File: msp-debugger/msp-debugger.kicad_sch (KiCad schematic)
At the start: 12 parts, among them J1 USB_B_Mini, J2 Conn_02x10, SW1 SW_MEC_5E, SW2 SW_MEC_5E, SW3 SW_MEC_5E, SW4 SW_MEC_5E, U1 ESP32-WROOM-32, U2 NHD-0420H1Z

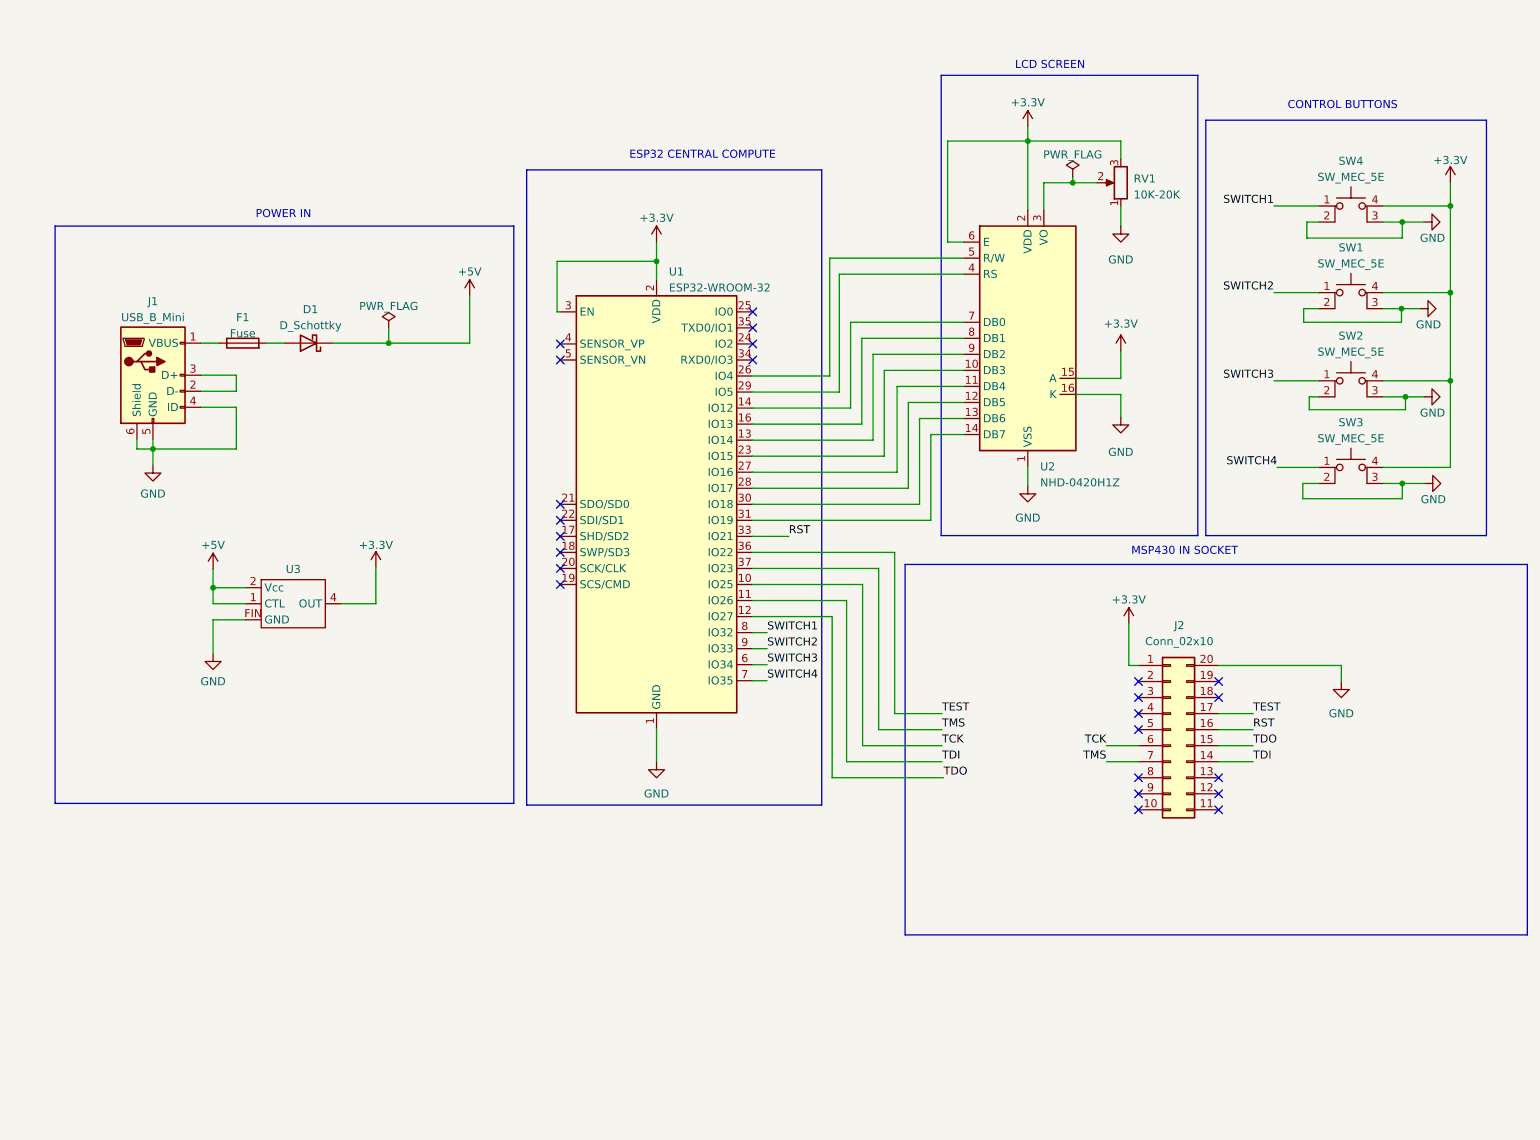
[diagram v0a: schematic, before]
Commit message: use digikey/espressif libraries
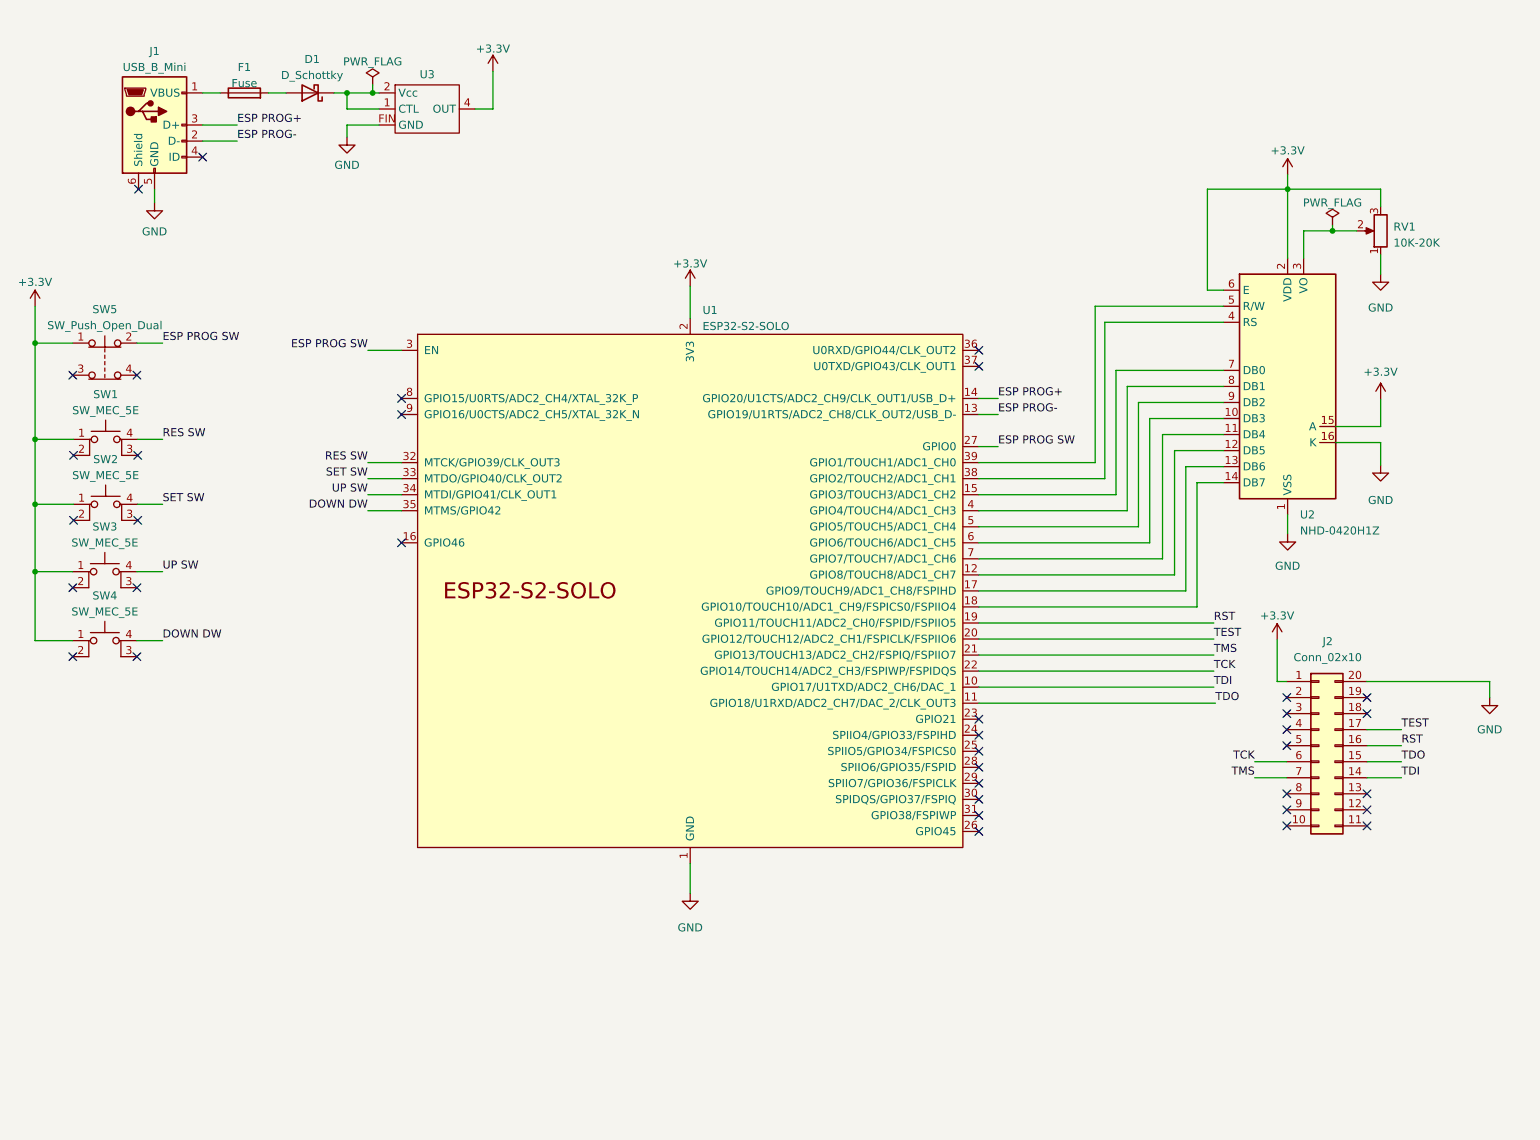
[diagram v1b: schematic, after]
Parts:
- removed U1: ESP32-WROOM-32, RF_Module:ESP32-WROOM-32, symbol RF_Module:ESP32-WROOM-32
- added SW5: SW_Push_Open_Dual, symbol Switch:SW_Push_Open_Dual
- added U1: ESP32-S2-SOLO, Espressif:ESP32-S2-SOLO, symbol Espressif:ESP32-S2-SOLO
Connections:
- net SWITCH1 is gone; now on net +3.3V: SW4.1
- net SWITCH2 is gone; now on net +3.3V: SW1.1
- net SWITCH3 is gone; now on net +3.3V: SW2.1
- net SWITCH4 is gone; now on net +3.3V: SW3.1
- net +3.3V: now also SW5.1, U1.2 (3V3); no longer SW1.4 (A), SW2.4 (A), SW3.4 (A), SW4.4 (A)
- net GND: now also U1.1 (GND), U1.40 (GND), U1.41 (GND); no longer J1.4 (ID), J1.6 (Shield), SW1.2, SW1.3 (K), SW2.2, SW2.3 (K), SW3.2, SW3.3 (K), SW4.2, SW4.3 (K)
- net RST: now also U1.19 (GPIO11/TOUCH11/ADC2_CH0/FSPID/FSPIIO5)
- net TCK: now also U1.22 (GPIO14/TOUCH14/ADC2_CH3/FSPIWP/FSPIDQS)
- net TDI: now also U1.10 (GPIO17/U1TXD/ADC2_CH6/DAC_1)
- net TDO: now also U1.11 (GPIO18/U1RXD/ADC2_CH7/DAC_2/CLK_OUT3)
- net TEST: now also U1.20 (GPIO12/TOUCH12/ADC2_CH1/FSPICLK/FSPIIO6)
- net TMS: now also U1.21 (GPIO13/TOUCH13/ADC2_CH2/FSPIQ/FSPIIO7)
- net at U2.9 (DB2): now also U1.5 (GPIO5/TOUCH5/ADC1_CH4)
- net at U2.7 (DB0): now also U1.15 (GPIO3/TOUCH3/ADC1_CH2)
- net at U2.8 (DB1): now also U1.4 (GPIO4/TOUCH4/ADC1_CH3)
- net at U2.10 (DB3): now also U1.6 (GPIO6/TOUCH6/ADC1_CH5)
- net at U2.5 (R/W): now also U1.39 (GPIO1/TOUCH1/ADC1_CH0)
- net at U2.11 (DB4): now also U1.7 (GPIO7/TOUCH7/ADC1_CH6)
- net at U2.12 (DB5): now also U1.12 (GPIO8/TOUCH8/ADC1_CH7)
- net at U2.4 (RS): now also U1.38 (GPIO2/TOUCH2/ADC1_CH1)
- net at U2.13 (DB6): now also U1.17 (GPIO9/TOUCH9/ADC1_CH8/FSPIHD)
- net at U2.14 (DB7): now also U1.18 (GPIO10/TOUCH10/ADC1_CH9/FSPICS0/FSPIIO4)
- net ESP PROG+: now reaches J1.3 (D+)
- net ESP PROG+: now also U1.14 (GPIO20/U1CTS/ADC2_CH9/CLK_OUT1/USB_D+); no longer J1.2 (D-)
- net +5V: no longer names the net of D1.1 (K), U3.1 (CTL), U3.2 (Vcc)
- new net DOWN DW: SW4.4 (A), U1.35 (MTMS/GPIO42)
- new net ESP PROG SW: SW5.2, U1.27 (GPIO0), U1.3 (EN)
- new net ESP PROG-: J1.2 (D-), U1.13 (GPIO19/U1RTS/ADC2_CH8/CLK_OUT2/USB_D-)
- new net RES SW: SW1.4 (A), U1.32 (MTCK/GPIO39/CLK_OUT3)
- new net SET SW: SW2.4 (A), U1.33 (MTDO/GPIO40/CLK_OUT2)
- new net UP SW: SW3.4 (A), U1.34 (MTDI/GPIO41/CLK_OUT1)
- no-connect marks 24 -> 37
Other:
- note removed: "CONTROL BUTTONS"
- note removed: "ESP32 CENTRAL COMPUTE"
- note removed: "LCD SCREEN"
- note removed: "MSP430 IN SOCKET"
- note removed: "POWER IN"
- moved on the sheet: D1, F1, J1, J2, RV1, U2, U3

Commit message: finalize schematic
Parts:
- removed D1: D_Schottky, Diode_SMD:D_SOD-128, symbol Device:D_Schottky
- removed J1: USB_B_Mini, symbol Connector:USB_B_Mini
- removed SW5: SW_Push_Open_Dual, symbol Switch:SW_Push_Open_Dual
- added C1: 1uF, symbol Device:C
- added C2, C5, C6: 0.1uF, symbol Device:C
- added C3, C4: 10uF, symbol Device:C
- added D1: D, symbol Device:D
- added J1: USB_B_Micro, symbol Connector:USB_B_Micro
- added R1: 10k, symbol Device:R
- added SW5, SW6: SW_MEC_5E, symbol Switch:SW_MEC_5E
- U3: value ~ -> BA033CC0FP-E2
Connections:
- net +3.3V: now also C1.1, C2.1, C3.1, D1.2 (A), R1.1
- net ESP PROG SW: now also C6.1, SW6.4 (A); no longer U1.3 (EN)
- net GND: now also C1.2, C2.2, C3.2, C4.2, C5.2, C6.2, J1.5 (GND), J1.6 (Shield), SW5.1, SW6.1
- net DB3: now reaches U1.6 (GPIO6/TOUCH6/ADC1_CH5), U2.10 (DB3)
- net DB4: now reaches U1.7 (GPIO7/TOUCH7/ADC1_CH6), U2.11 (DB4)
- net DB5: now reaches U1.12 (GPIO8/TOUCH8/ADC1_CH7), U2.12 (DB5)
- net DB6: now reaches U1.17 (GPIO9/TOUCH9/ADC1_CH8/FSPIHD), U2.13 (DB6)
- net DB7: now reaches U1.18 (GPIO10/TOUCH10/ADC1_CH9/FSPICS0/FSPIIO4), U2.14 (DB7)
- net LCD RS: now reaches U1.38 (GPIO2/TOUCH2/ADC1_CH1), U2.4 (RS)
- net LCD R/W: now reaches U1.39 (GPIO1/TOUCH1/ADC1_CH0), U2.5 (R/W)
- net DB0: now reaches U1.15 (GPIO3/TOUCH3/ADC1_CH2), U2.7 (DB0)
- net DB1: now reaches U1.4 (GPIO4/TOUCH4/ADC1_CH3), U2.8 (DB1)
- net DB2: now reaches U1.5 (GPIO5/TOUCH5/ADC1_CH4), U2.9 (DB2)
- net at U3.2 (VIN): now also F1.2, C4.1, D1.1 (K); no longer U3.1 (CTL)
- net at F1.1: now also J1.1 (VBUS)
- net ESP PROG+ renamed D+
- net D+: now also J1.3 (D+)
- net ESP PROG- renamed D-
- net D-: now also J1.2 (D-)
- new net ESP EN: C5.1, R1.2, SW5.4 (A), U1.3 (EN)
- no-connect marks 37 -> 38
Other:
- note added: "CENTRAL COMPUTE"
- note added: "CONTROL BUTTONS"
- note added: "LCD SCREEN"
- note added: "MSP430G2553IN20 SOCKET"
- note added: "POWER"
- note added: "PROGRAMMING BUTTONS"
- moved on the sheet: F1, J2, RV1, SW1, SW2, SW3, SW4, U1, U2

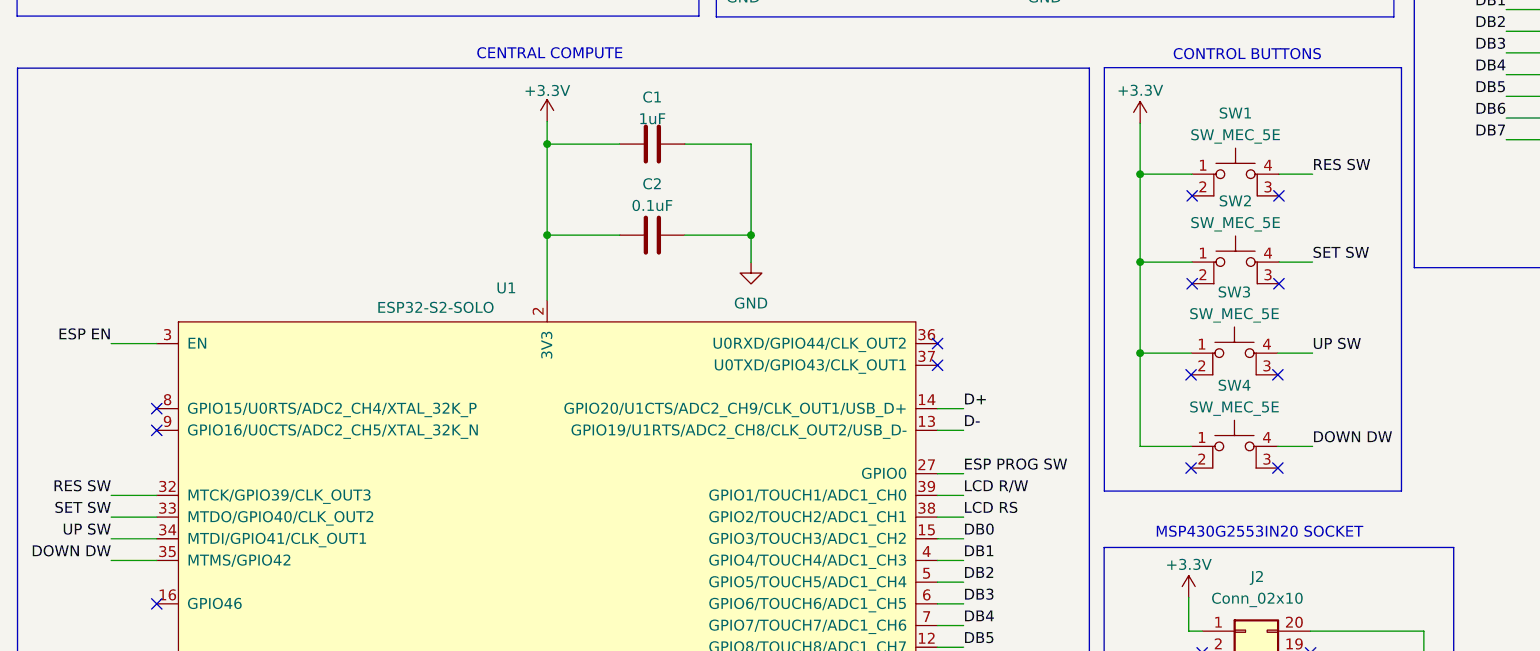
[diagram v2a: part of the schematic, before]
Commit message: update components & footprints
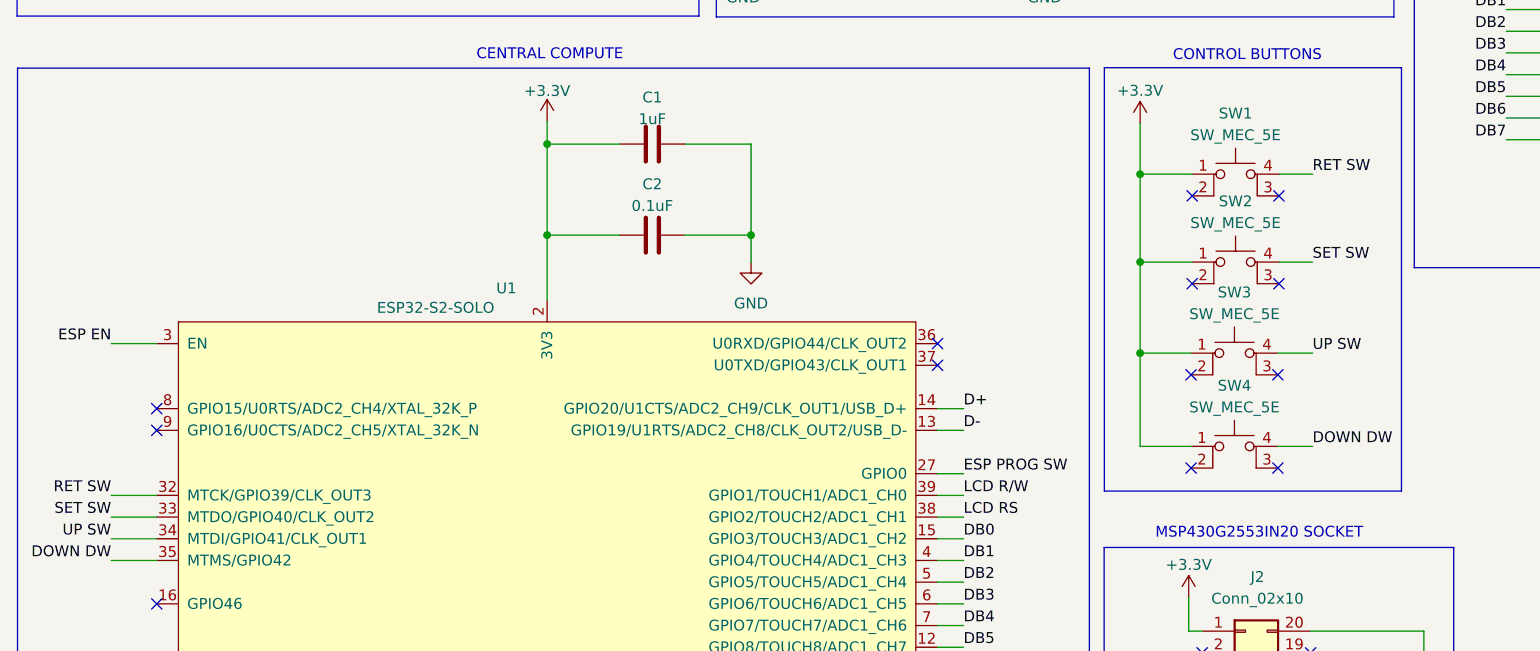
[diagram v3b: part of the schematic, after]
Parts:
- C1, C2, C3, C4, C5, C6: footprint (none) -> Capacitor_SMD:C_0805_2012Metric
- D1: footprint (none) -> Diode_SMD:D_SMA
- J1: footprint (none) -> Connector_USB:USB_Micro-B_Amphenol_10118194_Horizontal
- R1: footprint (none) -> Resistor_SMD:R_0805_2012Metric
- U3: footprint (none) -> digikey-footprints:TO-252-3
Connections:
- net RES SW renamed RET SW
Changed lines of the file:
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@@
     (effects (font (size 1.27 1.27)) (justify left bottom))
   )
-  (label "RES SW" (at 192.2526 80.137 0) (fields_autoplaced)
+  (label "RET SW" (at 192.2526 80.137 0) (fields_autoplaced)
     (effects (font (size 1.27 1.27)) (justify left bottom))
   )
@@
     (effects (font (size 1.27 1.27)) (justify right bottom))
   )
-  (label "RES SW" (at 51.562 117.7544 180) (fields_autoplaced)
+  (label "RET SW" (at 51.562 117.7544 180) (fields_autoplaced)
     (effects (font (size 1.27 1.27)) (justify right bottom))
   )
@@
       (effects (font (size 1.27 1.27)))
     )
-    (property "Footprint" "" (at 94.5388 28.448 0)
+    (property "Footprint" "Diode_SMD:D_SMA" (at 94.5388 28.448 0)
       (effects (font (size 1.27 1.27)) hide)
     )
@@
       (effects (font (size 1.27 1.27)))
     )
-    (property "Footprint" "" (at 168.7068 51.562 0)
+    (property "Footprint" "Capacitor_SMD:C_0805_2012Metric" (at 168.7068 51.562 0)
       (effects (font (size 1.27 1.27)) hide)
     )
@@
       (effects (font (size 1.27 1.27)))
     )
-    (property "Footprint" "" (at 118.745 86.3092 0)
+    (property "Footprint" "Capacitor_SMD:C_0805_2012Metric" (at 118.745 86.3092 0)
       (effects (font (size 1.27 1.27)) hide)
     )
@@
       (effects (font (size 1.27 1.27)) (justify left))
     )
-    (property "Footprint" "" (at 69.0372 46.7614 0)
+    (property "Footprint" "Capacitor_SMD:C_0805_2012Metric" (at 69.0372 46.7614 0)
       (effects (font (size 1.27 1.27)) hide)
     )
@@
       (effects (font (size 1.27 1.27)) (justify left))
     )
-    (property "Footprint" "" (at 144.78 31.6484 90)
+    (property "Footprint" "Resistor_SMD:R_0805_2012Metric" (at 144.78 31.6484 90)
       (effects (font (size 1.27 1.27)) hide)
     )
@@
       (effects (font (size 1.27 1.27)) (justify left))
     )
-    (property "Footprint" "" (at 112.7252 49.276 0)
+    (property "Footprint" "Capacitor_SMD:C_0805_2012Metric" (at 112.7252 49.276 0)
       (effects (font (size 1.27 1.27)) hide)
     )
@@
       (effects (font (size 1.27 1.27)))
     )
-    (property "Footprint" "" (at 133.4008 51.562 0)
+    (property "Footprint" "Capacitor_SMD:C_0805_2012Metric" (at 133.4008 51.562 0)
       (effects (font (size 1.27 1.27)) hide)
     )
@@
       (effects (font (size 1.27 1.27)))
     )
-    (property "Footprint" "" (at 93.1672 37.9476 0)
+    (property "Footprint" "digikey-footprints:TO-252-3" (at 93.1672 37.9476 0)
       (effects (font (size 1.27 1.27)) hide)
     )
@@
       (effects (font (size 1.27 1.27)))
     )
-    (property "Footprint" "" (at 52.07 36.9824 0)
+    (property "Footprint" "Connector_USB:USB_Micro-B_Amphenol_10118194_Horizontal" (at 52.07 36.9824 0)
       (effects (font (size 1.27 1.27)) hide)
     )
@@
       (effects (font (size 1.27 1.27)))
     )
-    (property "Footprint" "" (at 118.745 75.6412 0)
-      (effects (font (size 1.27 1.27)) hide)
-    )
+    (property "Footprint" "Capacitor_SMD:C_0805_2012Metric" (at 118.745 75.6412 0)
+      (effects (font (size 1.27 1.27)) hide)
+    )
